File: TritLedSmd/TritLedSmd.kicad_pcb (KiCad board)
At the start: 2 copper layers, 22.2 x 16.5 mm, 10 parts, among them P1 Power, P2 In, U1 LM393

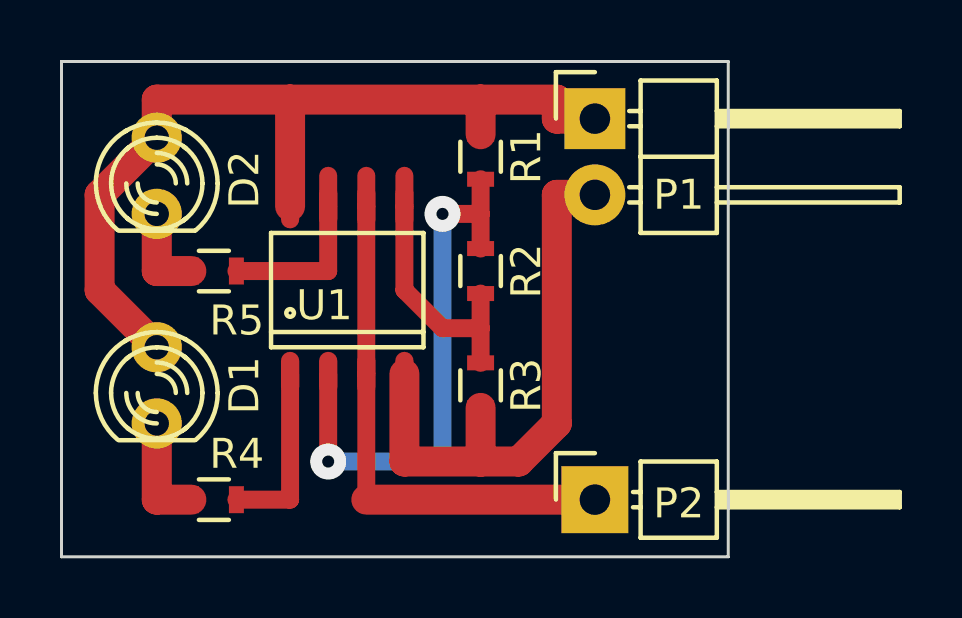
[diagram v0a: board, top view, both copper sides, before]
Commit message: 3D вид и исправление расположения элементов
Signed-off-by: Angel <angel@skynet.bank.srv>
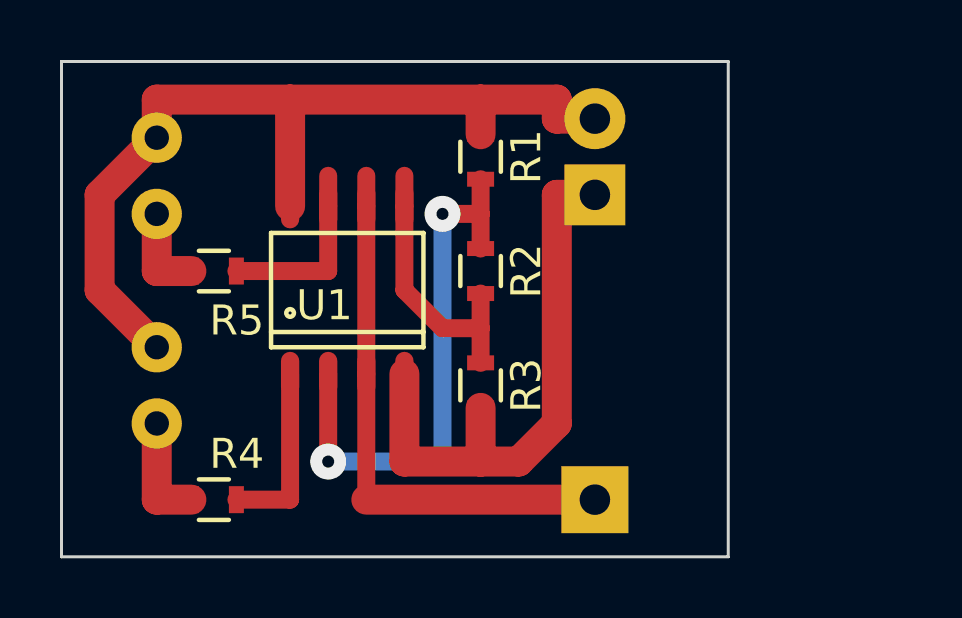
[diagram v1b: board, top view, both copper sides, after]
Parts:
- D1, D2, P1, P2: moved to B.Cu
- moved P1 2.54 mm to (50.8, 22.9)
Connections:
- P1 pad 1: Net-(D1-Pad1) -> Net-(P1-Pad1)
- P1 pad 2: Net-(P1-Pad2) -> Net-(D1-Pad1)
- R3 pad 2: Net-(P1-Pad2) -> Net-(P1-Pad1)
- U1 pad 4: Net-(P1-Pad2) -> Net-(P1-Pad1)
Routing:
- net Net-(P1-Pad2): track 19.2 -> 0.00 mm
- net Net-(P1-Pad1): track 0.00 -> 19.2 mm

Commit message: Косметические правки изображений
Signed-off-by: Алексей Кляузер <drum@pisem.net>
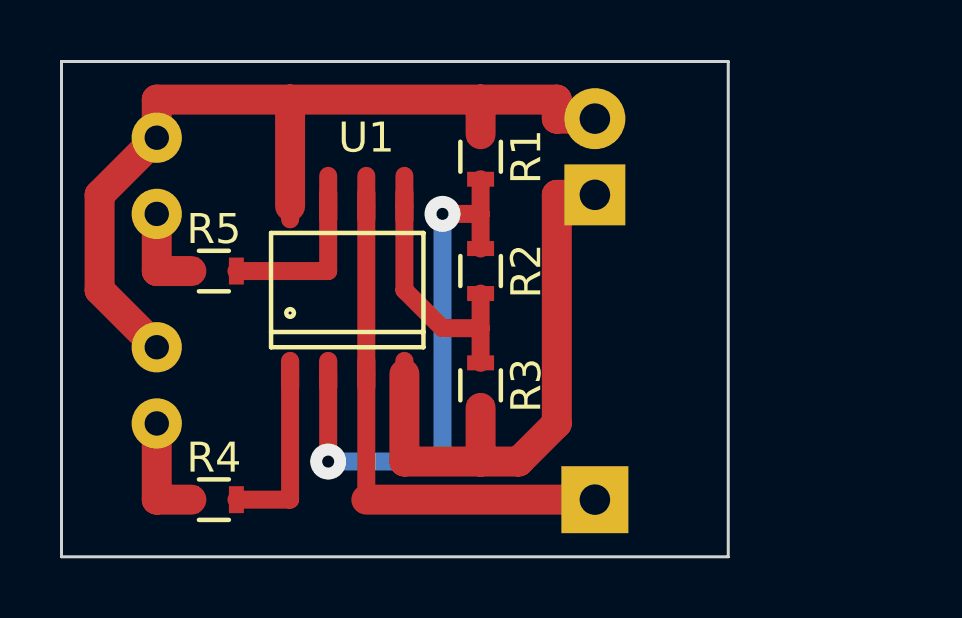
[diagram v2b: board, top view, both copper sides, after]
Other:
- board text added: "+"
- board text added: "+2,5В"
- board text added: "-"
- board text added: "-2,5В"
- board text added: "Trit"
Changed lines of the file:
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@@
-(kicad_pcb (version 4) (host pcbnew "(after 2015-mar-04 BZR unknown)-product")
+(kicad_pcb (version 4) (host pcbnew 0.201504271001+5626~23~ubuntu15.04.1-product)
   (general
     (links 16)
@@
     (area 32.969999 18.364999 55.295001 34.975001)
     (thickness 1.6)
-    (drawings 4)
+    (drawings 9)
     (tracks 45)
     (zones 0)
@@
     (34 B.Paste user hide)
     (35 F.Paste user hide)
-    (36 B.SilkS user hide)
+    (36 B.SilkS user)
     (37 F.SilkS user)
     (38 B.Mask user hide)
@@
     (descr "LED 3mm - Lead pitch 100mil (2,54mm)")
     (tags "LED led 3mm 3MM 100mil 2,54mm")
-    (fp_text reference D1 (at 0 -2.54 270) (layer B.SilkS)
-      (effects (font (size 1 1) (thickness 0.15)) (justify mirror))
-    )
-    (fp_text value - (at -1.27 1.905 540) (layer B.Fab)
+    (fp_text reference D1 (at 0 -3.175 270) (layer B.SilkS)
+      (effects (font (size 1 1) (thickness 0.15)) (justify mirror))
+    )
+    (fp_text value - (at 3.175 1.905 270) (layer B.Fab)
       (effects (font (size 1 1) (thickness 0.15)) (justify mirror))
     )
@@
     (descr "LED 3mm - Lead pitch 100mil (2,54mm)")
     (tags "LED led 3mm 3MM 100mil 2,54mm")
-    (fp_text reference D2 (at 0 -2.54 270) (layer B.SilkS)
-      (effects (font (size 1 1) (thickness 0.15)) (justify mirror))
-    )
-    (fp_text value + (at -1.905 1.905 540) (layer B.Fab)
+    (fp_text reference D2 (at 0 -3.175 270) (layer B.SilkS)
+      (effects (font (size 1 1) (thickness 0.15)) (justify mirror))
+    )
+    (fp_text value + (at 3.175 1.905 540) (layer B.Fab)
       (effects (font (size 1 1) (thickness 0.15)) (justify mirror))
     )
@@
     (descr "Through hole pin header")
     (tags "pin header")
-    (fp_text reference P2 (at 0.635 -2.54 90) (layer B.SilkS)
-      (effects (font (size 1 1) (thickness 0.15)) (justify mirror))
-    )
-    (fp_text value In (at 2.54 0 90) (layer B.Fab)
+    (fp_text reference P2 (at 2.794 -2.921 90) (layer B.SilkS)
+      (effects (font (size 1 1) (thickness 0.15)) (justify mirror))
+    )
+    (fp_text value In (at 6.985 -6.35) (layer B.Fab) hide
       (effects (font (size 1 1) (thickness 0.15)) (justify mirror))
     )
@@
     (descr "SO-8 Surface Mount Small Outline 150mil 8pin Package")
     (tags "Power Integrations D Package")
-    (fp_text reference U1 (at -0.762 0.508) (layer F.SilkS)
-      (effects (font (size 1 1) (thickness 0.15)))
-    )
-    (fp_text value LM393 (at 0.127 -1.016) (layer F.Fab)
+    (fp_text reference U1 (at 0.635 -5.08) (layer F.SilkS)
+      (effects (font (size 1 1) (thickness 0.15)))
+    )
+    (fp_text value LM393 (at 15.875 0.635) (layer F.Fab) hide
       (effects (font (size 1 1) (thickness 0.15)))
     )
@@
     (descr "Through hole pin header")
     (tags "pin header")
-    (fp_text reference P1 (at 0.635 2.54 90) (layer B.SilkS)
-      (effects (font (size 1 1) (thickness 0.15)) (justify mirror))
-    )
-    (fp_text value Power (at 2.54 -0.635 90) (layer B.Fab)
+    (fp_text reference P1 (at 2.794 2.921 90) (layer B.SilkS)
+      (effects (font (size 1 1) (thickness 0.15)) (justify mirror))
+    )
+    (fp_text value Power (at 7.62 3.81) (layer B.Fab) hide
       (effects (font (size 1 1) (thickness 0.15)) (justify mirror))
     )
@@
       (effects (font (size 1 1) (thickness 0.15)))
     )
-    (fp_text value 4.7KΩ (at 0.635 16.51 540) (layer F.Fab) hide
+    (fp_text value 4.7KΩ (at 5.08 -10.795 540) (layer F.Fab) hide
       (effects (font (size 1 1) (thickness 0.15)))
     )
@@
     (tags "resistor 0603")
     (attr smd)
-    (fp_text reference R4 (at 0.762 -1.524) (layer F.SilkS)
-      (effects (font (size 1 1) (thickness 0.15)))
-    )
-    (fp_text value 220Ω (at -7.366 -12.446) (layer F.Fab) hide
+    (fp_text reference R4 (at 0 -1.397) (layer F.SilkS)
+      (effects (font (size 1 1) (thickness 0.15)))
+    )
+    (fp_text value 220Ω (at 19.685 -6.35) (layer F.Fab) hide
       (effects (font (size 1 1) (thickness 0.15)))
     )
@@
       (effects (font (size 1 1) (thickness 0.15)))
     )
-    (fp_text value 4.7KΩ (at -1.651 16.51 360) (layer F.Fab) hide
+    (fp_text value 4.7KΩ (at 1.27 -11.43 360) (layer F.Fab) hide
       (effects (font (size 1 1) (thickness 0.15)))
     )
@@
       (effects (font (size 1 1) (thickness 0.15)))
     )
-    (fp_text value 4.7KΩ (at -3.81 16.51 360) (layer F.Fab) hide
+    (fp_text value 4.7KΩ (at -2.54 -11.43 360) (layer F.Fab) hide
       (effects (font (size 1 1) (thickness 0.15)))
     )
@@
     (tags "resistor 0603")
     (attr smd)
-    (fp_text reference R5 (at 0.762 1.651) (layer F.SilkS)
-      (effects (font (size 1 1) (thickness 0.15)))
-    )
-    (fp_text value 220Ω (at -7.366 -6.35) (layer F.Fab) hide
+    (fp_text reference R5 (at 0 -1.397) (layer F.SilkS)
+      (effects (font (size 1 1) (thickness 0.15)))
+    )
+    (fp_text value 220Ω (at 19.685 1.27) (layer F.Fab) hide
       (effects (font (size 1 1) (thickness 0.15)))
     )
@@
     )
   )
+  (gr_text Trit (at 47.244 33.401) (layer B.SilkS)
+    (effects (font (size 1.5 1.5) (thickness 0.3)) (justify mirror))
+  )
+  (gr_text +2,5В (at 46.99 19.685) (layer B.SilkS)
+    (effects (font (size 1 1) (thickness 0.1)) (justify mirror))
+  )
+  (gr_text -2,5В (at 46.99 22.225) (layer B.SilkS)
+    (effects (font (size 1 1) (thickness 0.1)) (justify mirror))
+  )
+  (gr_text + (at 34.29 25.4) (layer B.SilkS)
+    (effects (font (size 1.5 1.5) (thickness 0.3)) (justify mirror))
+  )
+  (gr_text - (at 34.29 32.385 90) (layer B.SilkS)
+    (effects (font (size 1.5 1.5) (thickness 0.3)) (justify mirror))
+  )
   (gr_line (start 33.02 18.415) (end 55.245 18.415) (angle 90) (layer Edge.Cuts) (width 0.1))
